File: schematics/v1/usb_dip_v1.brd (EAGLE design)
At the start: 41 x 50 mm, 41 parts, among them U1 PRTR5V0U2X, U2 PRTR5V0U2X, U3 PRTR5V0U2X, U4 PRTR5V0U2X

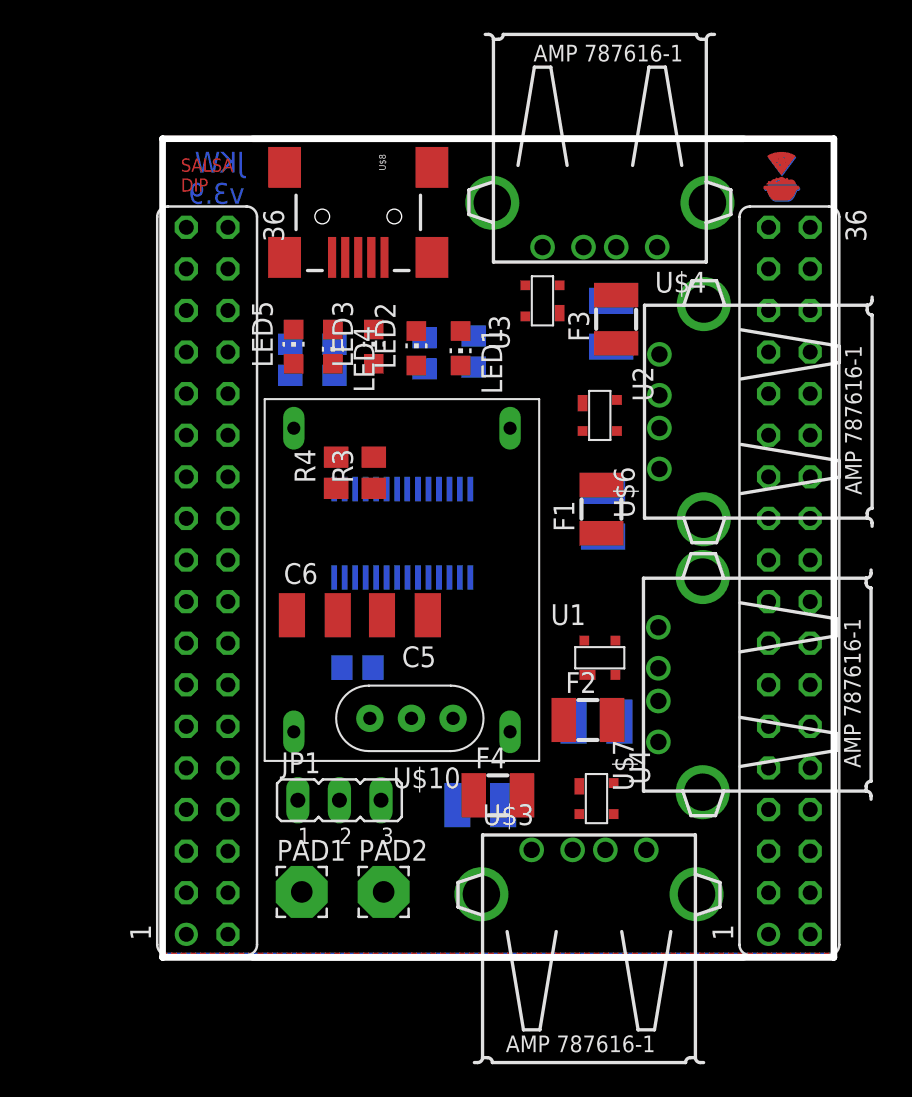
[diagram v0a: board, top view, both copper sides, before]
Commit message: Ordered Board v1 at OSH and seeed, renamed dev version
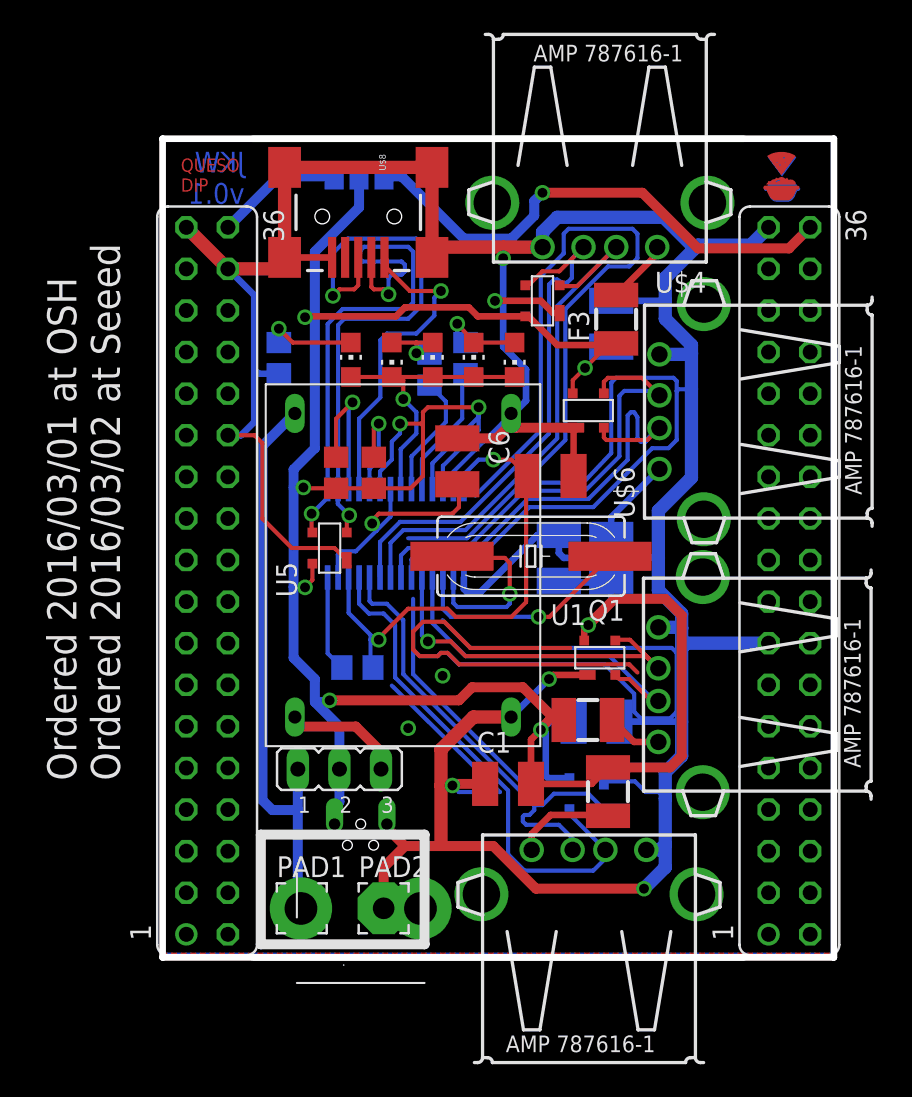
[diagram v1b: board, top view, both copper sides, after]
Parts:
- removed R2: ?, rcl:R0805
- added Q1: (no value), adafruit:SM49
- added SJ1: (no value), SparkFun-Retired:SJ_2
- added U5: PRTR5V0U2X, Volks73-NXPSemiconductors:SOT-143B
- U$10: value (none) -> USB-PWR; device adafruit:CERM_OSC -> adafruit:USB-MINIB-THM-MOLEX-PWRONLY
- moved U$9 28.4 mm to (6.30, 35.0), turned to 270 degrees
- moved C6 12.8 mm to (18.0, 30.3), turned to 270 degrees
- moved C5 12.3 mm to (23.7, 29.4)
- moved U$10 11.5 mm to (12.1, 3.50), turned to 0 degrees
- moved F4 6.70 mm to (27.2, 10.1), turned to 270 degrees
- moved R6 5.83 mm to (16.3, 35.9)
- moved C3 3.82 mm to (24.2, 24.4)
- moved LED3 3.69 mm to (16.5, 36.5)
- moved LED4 3.69 mm to (14.0, 36.5)
- moved LED5 3.59 mm to (11.5, 36.5)
- moved LED2 3.57 mm to (19.0, 36.5)
- moved LED1 3.37 mm to (21.5, 36.5)
- moved F1 3.06 mm to (27.4, 24.4), flipped to the bottom
- moved R5 2.52 mm to (18.5, 36.6)
- moved C1 2.14 mm to (21.1, 10.6), flipped to the top
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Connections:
- net N$1 renamed DM1
- net N$2 renamed DP1
- net N$26 renamed DM4
- net N$3 renamed DP3
- net N$4 renamed DM3
- net N$6 renamed DP4
- net N$7 renamed DP2
- net N$8 renamed DM2
- removed net N$20: U$1.16, U$8.D+
- removed net N$21: U$1.15, U$8.D-
- removed net N$23: R2.1, U$1.26
- new net CHR_IN: SJ1.1, SV2.36
- new net DMU: U$1.15, U$8.D-, U5.3
- new net DPU: U$1.16, U$8.D+, U5.2
- new net V_UP: U$1.18, U$8.VBUS
- net CHIP_5V: now also SJ1.3
- net GND: now also U$1.27, U$10.GND, U5.1; no longer U$10.P$2
- net N$27: now also Q1.2; no longer U$10.P$1
- net N$28: now also Q1.1; no longer U$10.P$3
- net VCC: now also SJ1.2, U$1.25, U$1.26, U$10.VBUS, U5.4; no longer R2.2, SV2.36
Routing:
- net GND: track 0.00 -> 412.1 mm, vias 0 -> 7
- net VCC: track 0.00 -> 165.7 mm, vias 0 -> 9
- net VIN: track 0.00 -> 35.4 mm
- net DMU: track 0.00 -> 34.5 mm, vias 0 -> 2
- net DPU: track 0.00 -> 34.4 mm, vias 0 -> 2
- net DP2: track 0.00 -> 32.8 mm
- net DM2: track 0.00 -> 32.7 mm
- net DP1: track 0.00 -> 31.8 mm
- net CHIP_5V: track 0.00 -> 31.2 mm, vias 0 -> 1
- net N$18: track 0.00 -> 30.7 mm, vias 0 -> 2
- net DM1: track 0.00 -> 29.5 mm
- net DP3: track 0.00 -> 28.2 mm
- net DM3: track 0.00 -> 27.9 mm
- net DP4: track 0.00 -> 23.5 mm, vias 0 -> 1
- net DM4: track 0.00 -> 21.8 mm
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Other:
- board text added: "JKW v0.1"
- board text added: "Ordered 2016/03/01 at OSH Ordered 2016/03/02 at Seeed"
- board text added: "QUESO DIP"
